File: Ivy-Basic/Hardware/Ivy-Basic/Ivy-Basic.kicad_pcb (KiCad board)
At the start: 2 copper layers, 8 parts, among them J1 USB_C_Receptacle_USB2.0_16P, U1 ESP32-S3-MINI-1, U2 TMC2208-LA

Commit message: I don't know what the diff is here
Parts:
- added C2: 10u, Capacitor_SMD:C_0603_1608Metric, F.Cu at (189.5, 48.9)
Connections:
- U1 pad 1: Net-(U1-GND-Pad1) -> GND
- U1 pad 2: Net-(U1-GND-Pad1) -> GND
- U1 pad 3: unconnected-(U1-3V3-Pad3) -> +3V3
- U1 pad 39: unconnected-(U1-TXD0-Pad39) -> TX
- U1 pad 4: unconnected-(U1-IO0-Pad4) -> Net-(U1-IO0)
- U1 pad 40: unconnected-(U1-RXD0-Pad40) -> RX
- U1 pad 42: Net-(U1-GND-Pad1) -> GND
- U1 pad 43: Net-(U1-GND-Pad1) -> GND
- U1 pad 45: unconnected-(U1-EN-Pad45) -> Net-(U1-EN)
- U1 pad 46: Net-(U1-GND-Pad1) -> GND
- U1 pad 47: Net-(U1-GND-Pad1) -> GND
- U1 pad 48: Net-(U1-GND-Pad1) -> GND
- U1 pad 49: Net-(U1-GND-Pad1) -> GND
- U1 pad 50: Net-(U1-GND-Pad1) -> GND
- U1 pad 51: Net-(U1-GND-Pad1) -> GND
- U1 pad 52: Net-(U1-GND-Pad1) -> GND
- U1 pad 53: Net-(U1-GND-Pad1) -> GND
- U1 pad 54: Net-(U1-GND-Pad1) -> GND
- U1 pad 55: Net-(U1-GND-Pad1) -> GND
- U1 pad 56: Net-(U1-GND-Pad1) -> GND
- U1 pad 57: Net-(U1-GND-Pad1) -> GND
- U1 pad 58: Net-(U1-GND-Pad1) -> GND
- U1 pad 59: Net-(U1-GND-Pad1) -> GND
- U1 pad 60: Net-(U1-GND-Pad1) -> GND
- U1 pad 61: Net-(U1-GND-Pad1) -> GND
- U1 pad 62: Net-(U1-GND-Pad1) -> GND
- U1 pad 63: Net-(U1-GND-Pad1) -> GND
- U1 pad 64: Net-(U1-GND-Pad1) -> GND
- U1 pad 65: Net-(U1-GND-Pad1) -> GND
- U2 pad 10: unconnected-(U2-MS2-Pad10) -> MS2_1
- U2 pad 11: unconnected-(U2-DIAG-Pad11) -> DIAG1
- U2 pad 12: unconnected-(U2-INDEX-Pad12) -> INDEX1
- U2 pad 13: unconnected-(U2-CLK-Pad13) -> /CLK
- U2 pad 14: unconnected-(U2-PDN_UART-Pad14) -> Net-(U2-PDN_UART)
- U2 pad 15: unconnected-(U2-VCC_IO-Pad15) -> +3V3
- U2 pad 16: unconnected-(U2-STEP-Pad16) -> STEP1
- U2 pad 18: Net-(U2-GND-Pad18) -> GND
- U2 pad 19: unconnected-(U2-DIR-Pad19) -> DIR1
- U2 pad 2: unconnected-(U2-ENN-Pad2) -> EN1
- U2 pad 22: Net-(U2-VS-Pad22) -> VBUS
- U2 pad 23: unconnected-(U2-BRA-Pad23) -> Net-(U2-BRA)
- U2 pad 27: unconnected-(U2-BRB-Pad27) -> Net-(U2-BRB)
- U2 pad 28: Net-(U2-VS-Pad22) -> VBUS
- U2 pad 3: Net-(U2-GND-Pad18) -> GND
- U2 pad 4: unconnected-(U2-CPO-Pad4) -> Net-(U2-CPO)
- U2 pad 5: unconnected-(U2-CPI-Pad5) -> Net-(U2-CPI)
- U2 pad 6: unconnected-(U2-VCP-Pad6) -> Net-(U2-VCP)
- U2 pad 8: unconnected-(U2-5VOUT-Pad8) -> Net-(U2-5VOUT)
- U2 pad 9: unconnected-(U2-MS1-Pad9) -> MS1_1

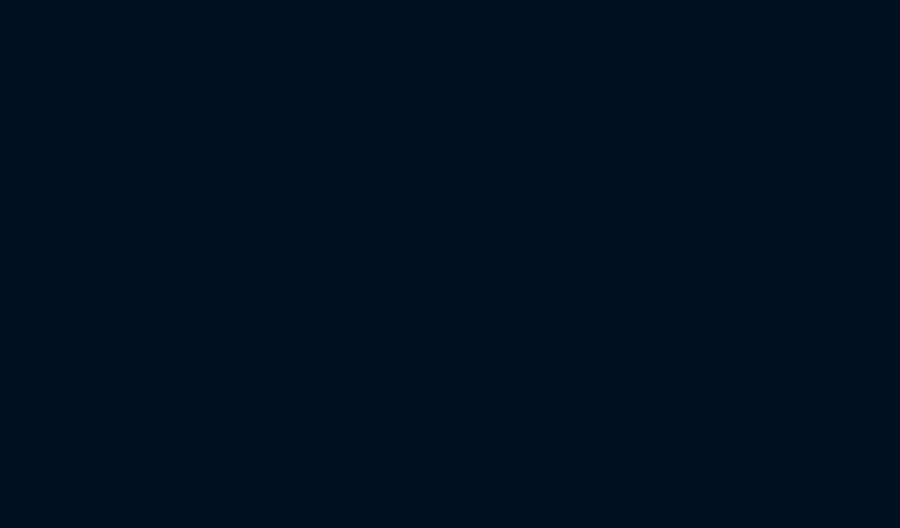
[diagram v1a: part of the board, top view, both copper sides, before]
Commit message: Replace buck converter with something that might work better
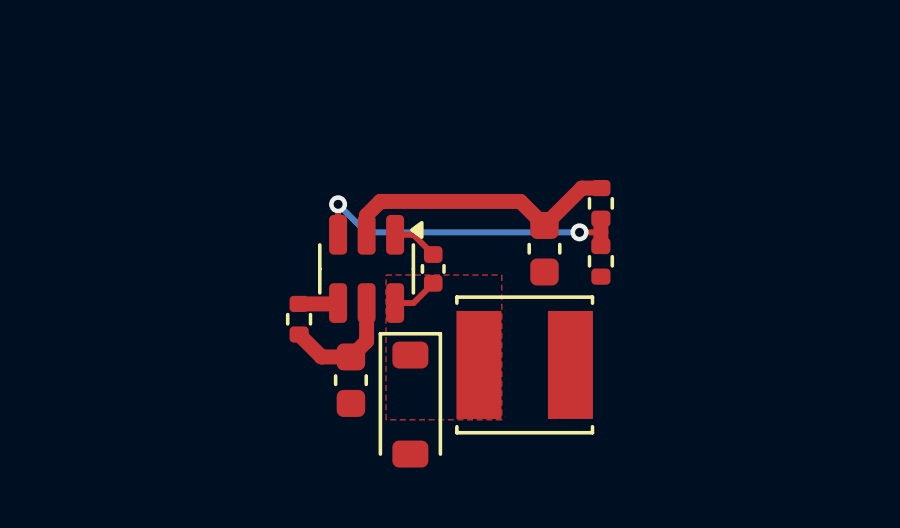
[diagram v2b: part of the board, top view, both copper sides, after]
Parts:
- added C10: 100n, Capacitor_SMD:C_0402_1005Metric, F.Cu at (152.5, 158.1)
- added C11: 4u7, Capacitor_SMD:C_0603_1608Metric, F.Cu at (149.7, 161.8)
- added C12: 10u, Capacitor_SMD:C_0603_1608Metric, F.Cu at (156.2, 157.5)
- added D1: D, Diode_SMD:D_SOD-123, F.Cu at (151.7, 162.7)
- added IC1: SSP9451, Package_TO_SOT_SMD:SOT-23-6, F.Cu at (150.2, 158.1)
- added L1: 3u3, Inductor_SMD:L_Abracon_ASPI-0425, F.Cu at (155.5, 161.3)
- added R10: 100k, Resistor_SMD:R_0402_1005Metric, F.Cu at (148.0, 159.8)
- added R5: 124k, Resistor_SMD:R_0402_1005Metric, F.Cu at (158.0, 157.9)
- added R6: 40k2, Resistor_SMD:R_0402_1005Metric, F.Cu at (158.0, 156.0)
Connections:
- net Net-(U2-5VOUT) renamed +5V
- U1 pad 11: unconnected-(U1-IO7-Pad11) -> DIAG1
- U1 pad 12: unconnected-(U1-IO8-Pad12) -> INDEX1
- U1 pad 14: unconnected-(U1-IO10-Pad14) -> EN1
- U1 pad 16: unconnected-(U1-IO12-Pad16) -> UART
- U1 pad 17: unconnected-(U1-IO13-Pad17) -> CLK
- U1 pad 5: unconnected-(U1-IO1-Pad5) -> MS1_1
- U1 pad 6: unconnected-(U1-IO2-Pad6) -> MS2_1
- U1 pad 8: unconnected-(U1-IO4-Pad8) -> STEP1
- U1 pad 9: unconnected-(U1-IO5-Pad9) -> DIR1
- U2 pad 1: unconnected-(U2-OB2-Pad1) -> OB2
- U2 pad 13: /CLK -> CLK
- U2 pad 14: Net-(U2-PDN_UART) -> UART
- U2 pad 17: unconnected-(U2-VREF-Pad17) -> Net-(U2-VREF)
- U2 pad 21: unconnected-(U2-OA2-Pad21) -> OA2
- U2 pad 24: unconnected-(U2-OA1-Pad24) -> OA1
- U2 pad 26: unconnected-(U2-OB1-Pad26) -> OB1
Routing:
- net FB: track 0.00 -> 11.1 mm, vias 0 -> 2
- net GND: track 0.00 -> 9.50 mm
- net VBUS: track 2.06 -> 6.11 mm
- net Net-(IC1-CB): track 0.00 -> 1.54 mm
- net Net-(D1-K): track 0.00 -> 1.54 mm
- net Net-(IC1-EN): track 0.00 -> 1.31 mm
- added copper zone on F.Cu, net Net-(D1-K)

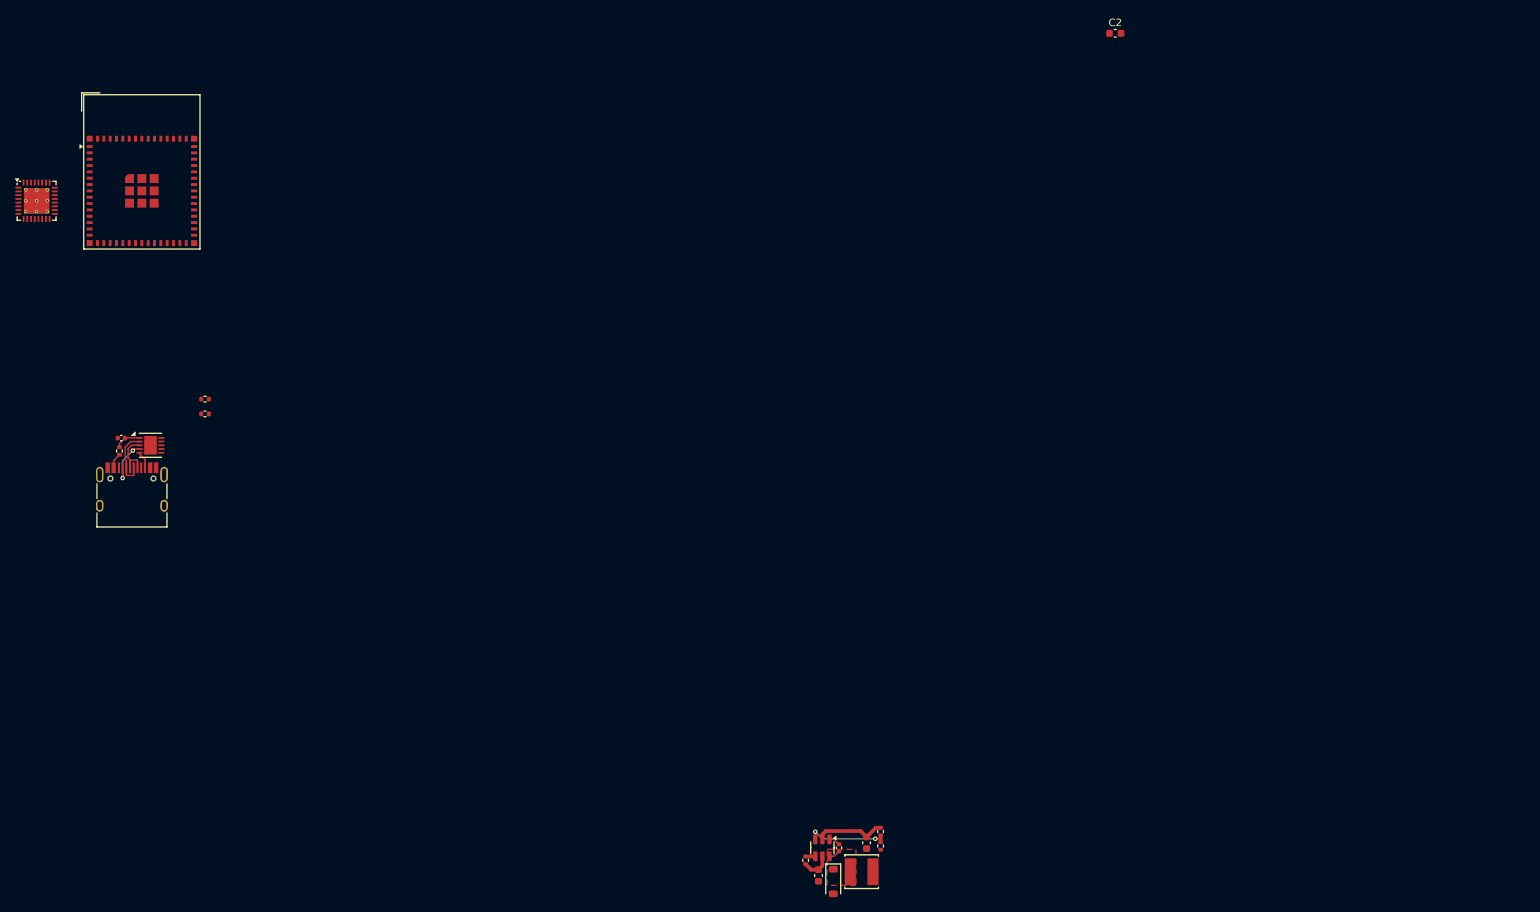
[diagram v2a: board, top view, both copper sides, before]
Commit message: Add 3D models, set board outline, place USB input, ESP32, Buck Converter
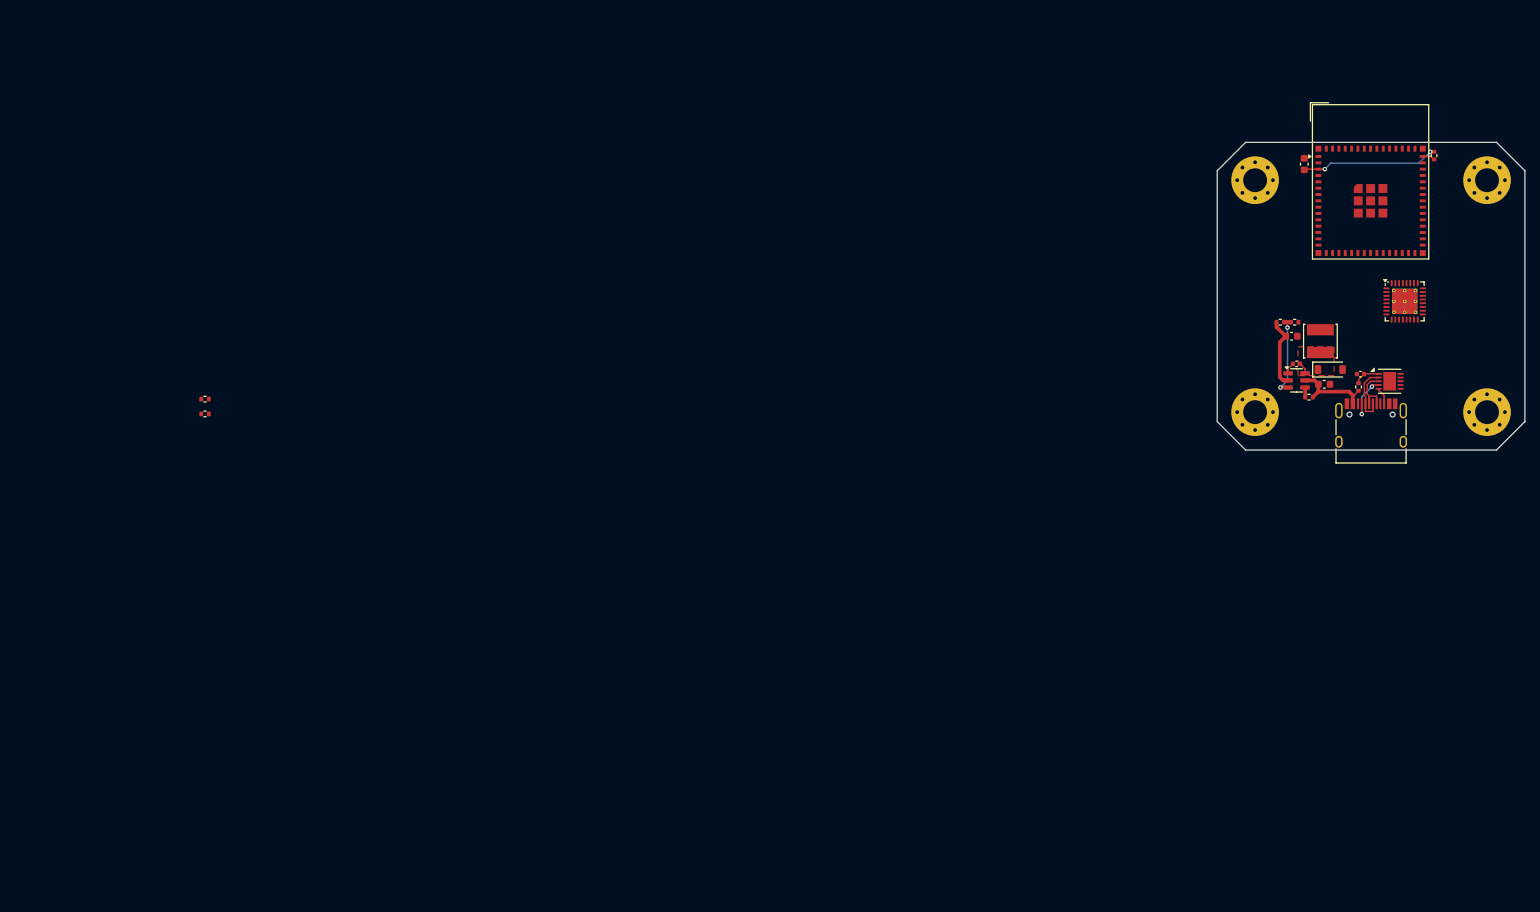
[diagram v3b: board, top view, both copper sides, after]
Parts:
- added R4: 10k, Resistor_SMD:R_0402_1005Metric, F.Cu at (232.3, 65.3)
- added REF**: MountingHole_3.2mm_M3_Pad_Via, MountingHole:MountingHole_3.2mm_M3_Pad_Via, F.Cu at (239.4, 99.7)
- added REF**: MountingHole_3.2mm_M3_Pad_Via, MountingHole:MountingHole_3.2mm_M3_Pad_Via, F.Cu at (208.3, 99.7)
- added REF**: MountingHole_3.2mm_M3_Pad_Via, MountingHole:MountingHole_3.2mm_M3_Pad_Via, F.Cu at (208.3, 68.6)
- added REF**: MountingHole_3.2mm_M3_Pad_Via, MountingHole:MountingHole_3.2mm_M3_Pad_Via, F.Cu at (239.4, 68.6)
- moved U2 184.0 mm to (228.3, 84.8)
- moved C1 166.5 mm to (222.4, 94.6)
- moved J1 166.5 mm to (223.8, 102.6)
- moved R1 166.5 mm to (222.2, 96.3)
- moved U3 166.5 mm to (226.3, 95.6)
- moved U1 164.8 mm to (223.8, 68.8)
- moved D1 95.7 mm to (218.4, 94.0), turned to 0 degrees
- moved C11 94.6 mm to (217.6, 96.0), turned to 180 degrees
- moved L1 94.1 mm to (217.0, 90.2), turned to 90 degrees
- moved R10 91.8 mm to (215.5, 97.7), turned to 0 degrees
- moved R5 89.6 mm to (213.6, 87.6), turned to 0 degrees
- moved C10 89.4 mm to (213.8, 93.2), turned to 0 degrees
- moved IC1 89.3 mm to (213.8, 95.4), turned to 0 degrees
- moved C12 88.7 mm to (213.2, 89.5), turned to 0 degrees
- moved R6 86.9 mm to (211.7, 87.6), turned to 0 degrees
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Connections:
- net /USB Power/D+ renamed D+
- net /USB Power/D- renamed D-
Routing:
- net +3V3: track 0.00 -> 18.4 mm, vias 0 -> 2
- net VBUS: track 6.11 -> 12.1 mm
- net Net-(U1-EN): track 0.00 -> 1.67 mm
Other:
- board outline added: 41.3 x 41.3 mm
